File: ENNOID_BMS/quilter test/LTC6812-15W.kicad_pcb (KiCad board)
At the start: 2 copper layers, 66 x 91.2 mm, 247 parts, among them J1 PB MB 2, J10 PB MB 1, J11 PA MA 1, J2 PA MA 2, J3 Sensors, J5 Cells, J6 Sensors, Q1 DZTT5551, Q10 TSM2323, Q11 TSM2323, Q12 TSM2323, Q13 TSM2323, Q14 TSM2323, Q15 TSM2323, Q16 TSM2323, Q17 DZTT5551, Q18 2N7002, Q19 2N7002, Q2 TSM2323, Q20 2N7002, Q21 2N7002, Q22 2N7002, Q23 2N7002, Q24 2N7002, Q25 2N7002, Q26 2N7002, Q27 2N7002, Q28 2N7002, Q29 2N7002, Q3 TSM2323, Q30 2N7002, Q31 2N7002, Q32 2N7002, Q4 TSM2323, Q5 TSM2323, Q6 TSM2323, Q7 TSM2323, Q8 TSM2323, Q9 TSM2323, U1 LTC6812-1, U2 LTC6812-1

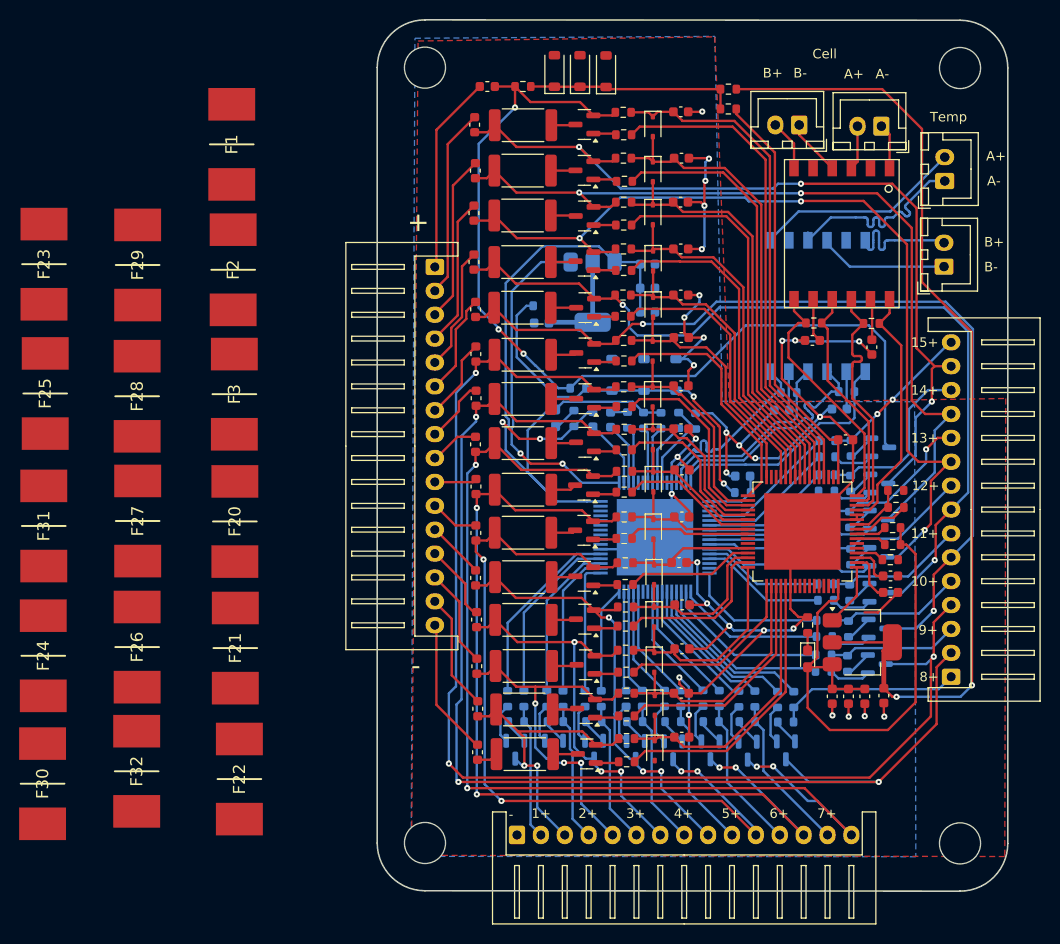
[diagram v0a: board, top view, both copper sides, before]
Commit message: slave with new fuses added
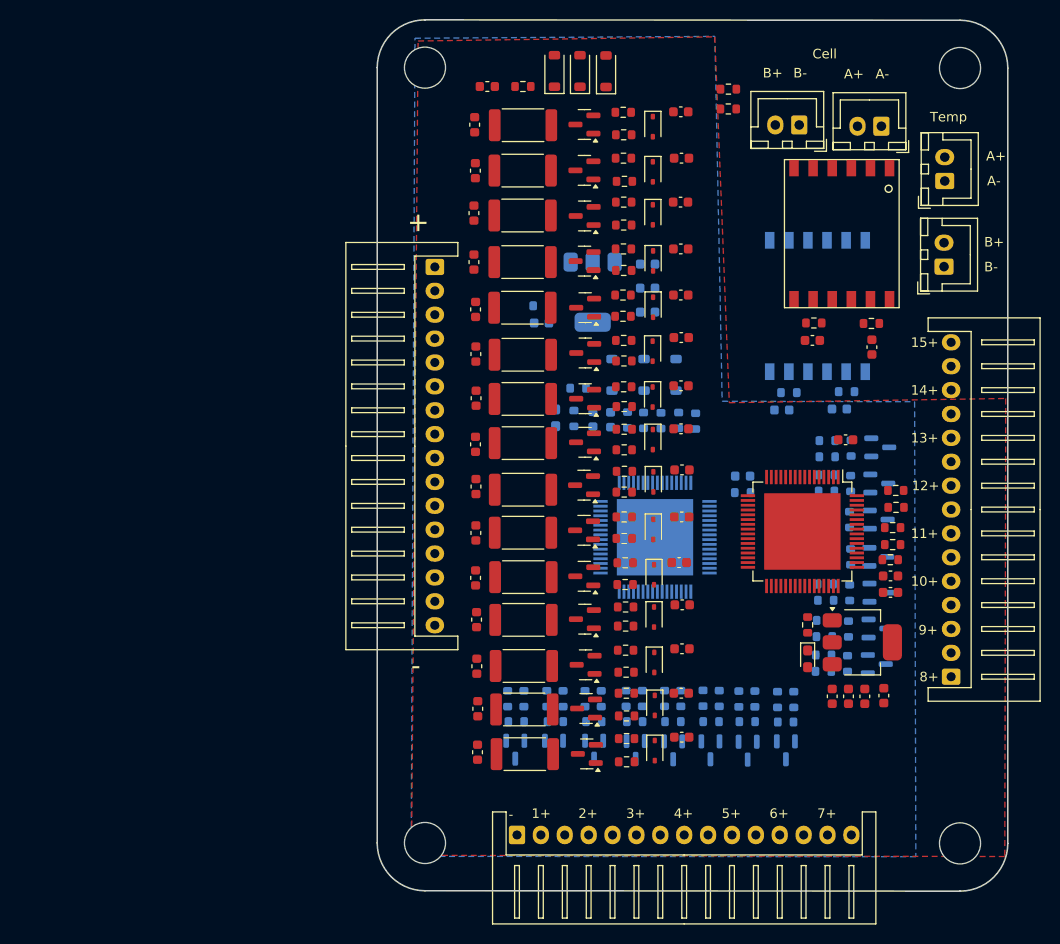
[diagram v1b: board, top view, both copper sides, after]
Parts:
- removed F1, F2, F20, F21, F22, F23, F24, F25, F26, F27, F28, F29, F3, F30, F31, F32: Fuse, ENNOID:FUSC10948X488N
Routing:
- net Cell_1-: track 211.9 -> 0.00 mm, vias 33 -> 0
- net Cell_9+: track 131.4 -> 0.00 mm, vias 3 -> 0
- net Cell_8+: track 128.3 -> 0.00 mm, vias 3 -> 0
- net Cell_7+: track 108.7 -> 0.00 mm, vias 4 -> 0
- net Net-(C4-Pad2): track 103.1 -> 0.00 mm, vias 2 -> 0
- net Cell_15+: track 99.5 -> 0.00 mm, vias 3 -> 0
- net Cell_6+: track 97.1 -> 0.00 mm, vias 4 -> 0
- net Cell_12+: track 95.0 -> 0.00 mm, vias 3 -> 0
- net Cell_10+: track 94.3 -> 0.00 mm, vias 2 -> 0
- net Cell_11+: track 90.7 -> 0.00 mm, vias 2 -> 0
- net Cell_13+: track 89.7 -> 0.00 mm, vias 2 -> 0
- net Cell_14+: track 88.5 -> 0.00 mm, vias 3 -> 0
- net Cell_5+: track 85.8 -> 0.00 mm, vias 4 -> 0
- net /Vreg_2: track 75.7 -> 0.00 mm
- net /Vreg_1: track 55.9 -> 0.00 mm
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
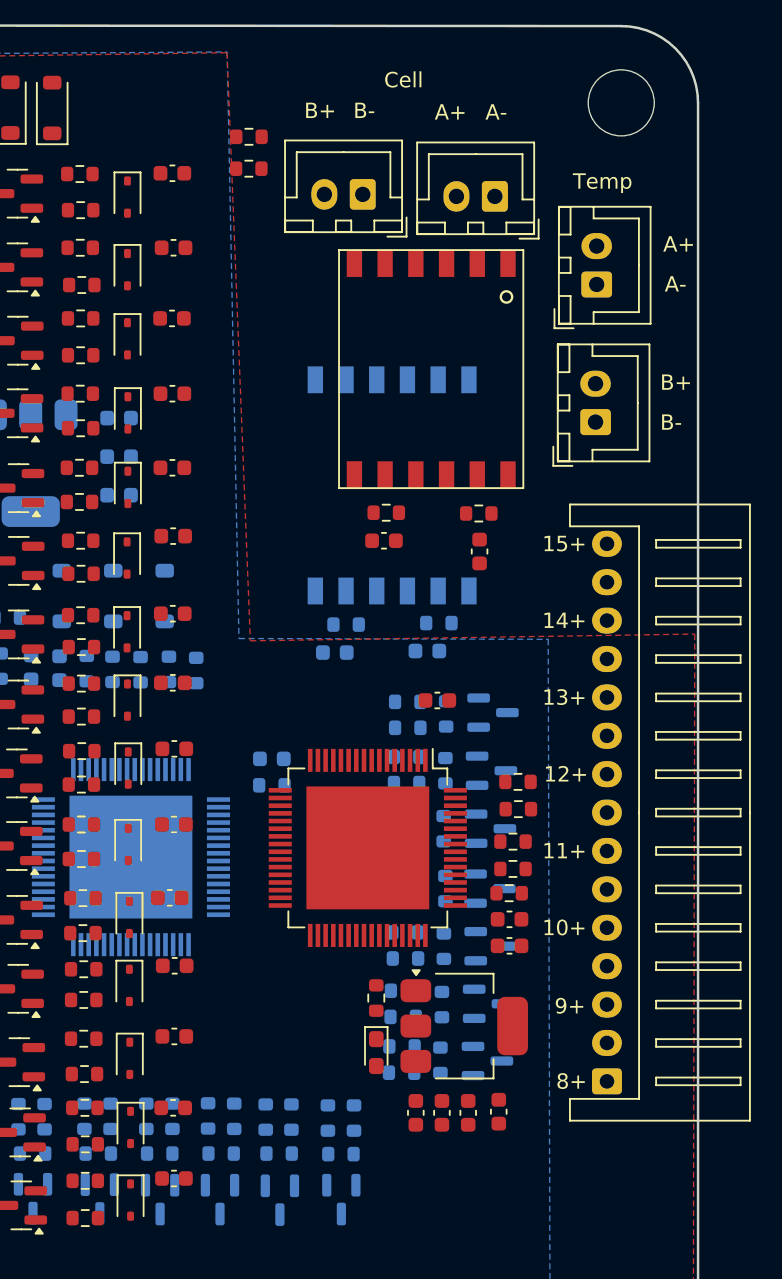
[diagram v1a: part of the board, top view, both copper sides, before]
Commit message: bms architecture notes made re charging and discharging
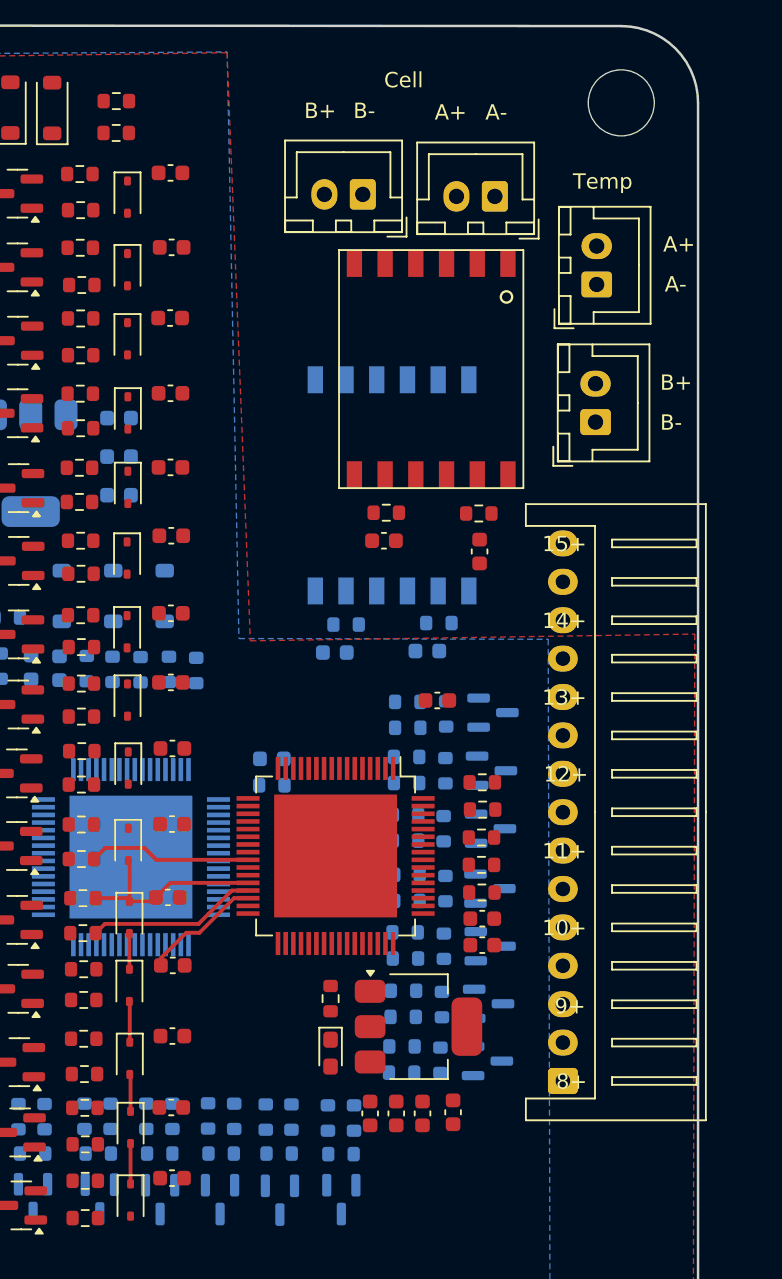
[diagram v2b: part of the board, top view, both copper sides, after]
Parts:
- moved R1 8.94 mm to (72.8, 42.4)
- moved R3 8.94 mm to (72.8, 40.3)
- moved C5 2.98 mm to (92.7, 106.2)
- moved C7 2.98 mm to (89.3, 106.2)
- moved D4 2.98 mm to (86.7, 102.3)
- moved R10 2.98 mm to (86.7, 98.7)
- moved C4 2.98 mm to (94.7, 106.1)
- moved C6 2.98 mm to (91.0, 106.2)
- moved Q1 2.98 mm to (92.5, 100.5)
- moved J3 2.87 mm to (101.8, 104.1)
- moved R2 2.33 mm to (96.6, 84.6)
- moved R5 2.33 mm to (96.6, 86.4)
- moved U1 2.16 mm to (87.0, 89.4)
- moved R4 2.07 mm to (96.5, 88.2)
- moved R6 2.07 mm to (96.5, 90.0)
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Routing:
- net /cell5/C: track 0.00 -> 13.2 mm
- net /cell5/S: track 0.00 -> 11.1 mm
- net /cell6/S: track 0.00 -> 10.6 mm
- net /cell4/C: track 0.00 -> 10.1 mm
- net /cell3/C: track 0.00 -> 2.66 mm
- net /cell1/C: track 0.00 -> 2.62 mm
- net /cell2/C: track 0.00 -> 2.42 mm
